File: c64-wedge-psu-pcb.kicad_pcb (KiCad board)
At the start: 2 copper layers, 70 x 57.5 mm, 23 parts, among them U1 LM2576T-ADJ

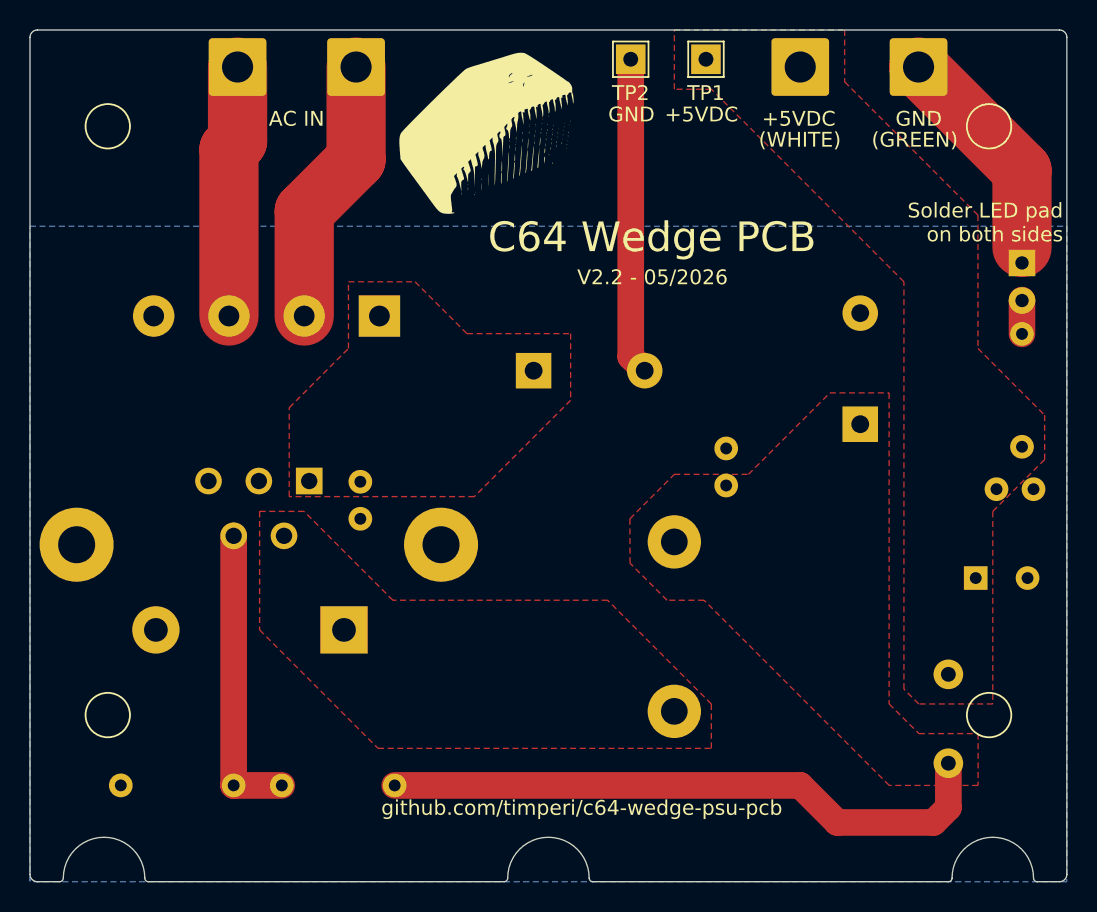
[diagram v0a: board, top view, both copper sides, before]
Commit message: created 3D model for heatsink + moved bridge rectifier + version number on PCB = 2.1.0
Changed heatsink to ATS-PCB1035 after measuring physical example and creating 3D model and footprint for it
Moved bridge rectifier after finding and fixing error in its KiCad 3D model
Changed version number on PCB to 2.1.0
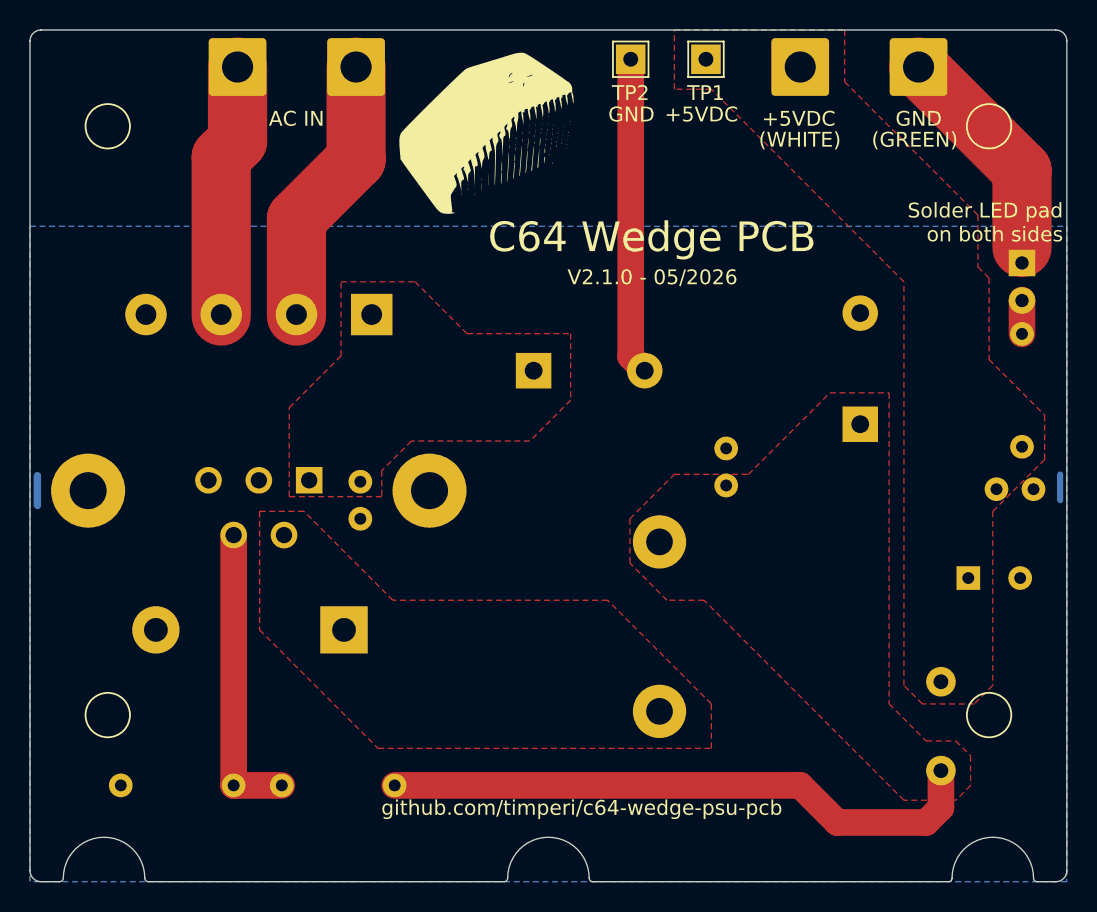
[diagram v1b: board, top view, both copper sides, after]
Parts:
- HS1: footprint c64-wedge-psu-pcb:ATS-PCB1036 -> c64-wedge-psu-pcb:ATS-PCB1035
- moved L1 1.00 mm to (132.5, 106.0)
- moved L2 0.71 mm to (151.5, 107.0)
- moved D1 0.53 mm to (113.1, 79.2)
- moved C3 0.50 mm to (153.3, 97.0)
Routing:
- net Net-(C2-Pad1): track 41.8 -> 40.8 mm
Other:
- outline, holes or cut-outs redrawn
- board text added: "4x Case PCB standoff"
- board text added: "Case PCB stop"
- board text added: "V2.1.0 - 05/2026"
- board text removed: "V2.2 - 05/2026"
